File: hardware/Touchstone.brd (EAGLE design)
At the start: 50.8 x 50.8 mm, 69 parts, among them J3 USB-MICROB, U1 NEOPIXEL_NANO_2427, U10 TSL2591, U11 915MHz, U12 MH-Z19, U13 CCS811-I2C, U14 IAQ-CORE-C, U15 VLP-450-F, U16 VLP-450-F, U2 FT231XQ-R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

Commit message: Added pullups on CCS811's signal lines
RESET AND WAKE lines pulled up by default
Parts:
- added R12, R14: 100K, Adafruit Feather 32u4 Bluefruit LE:MICROBUILDER__0402MP
- moved U13 0.25 mm to (40.2, 1.06)
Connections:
- new net N$6: R12.2, U13.2
- net D5: now also R14.2
- net VCC: now also R12.1, R14.1
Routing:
- net VCC: track 199.8 -> 212.9 mm, vias 7 -> 8
- net D5: track 42.6 -> 47.8 mm, vias 2 -> 3
- net N$6: track 0.00 -> 5.14 mm
- net N$13: track 11.6 -> 11.0 mm
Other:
- board text added: "v0.57 | August 2017"
- board text removed: "v0.56b | July 2017"

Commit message: Added SMD pads for T/RH breakout
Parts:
- added U$6: CONN_HDR_1.27MM_SMD_4POS, CONN_HDR_1.27MM_SMD_4POS:CONN_HDR_1.27MM_SMD_4POS
- moved U$3 17.5 mm to (33.5, 47.4)
- moved C16 6.83 mm to (45.7, 38.3)
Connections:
- net GND: now also U$6.P$4
- net SCL: now also U$6.P$2
- net SDA: now also U$6.P$3
- net VCC: now also U$6.P$1
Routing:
- net GND: track 21.3 -> 16.1 mm
- net VCC: track 212.9 -> 217.7 mm
- net SCL: track 165.8 -> 170.2 mm
- net SDA: track 160.1 -> 162.3 mm

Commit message: Version number change; minor adjustments
- Changed version number to 0.5.7 (new versioning format)
- silkscreen adjustments
- some schematic rearrangements
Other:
- board text added: "v0.5.7 | August 2017"
- board text removed: "v0.57 | August 2017"
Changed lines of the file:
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@@
 <text x="4.699" y="19.8628" size="1.016" layer="122" font="vector" ratio="16" rot="MR90" align="center-left">Touchstone</text>
 <text x="30.9372" y="49.5046" size="0.6096" layer="122" font="vector" rot="MR0">Designed by Akram Ali</text>
-<text x="3.0988" y="19.939" size="0.6096" layer="122" font="vector" rot="MR90">v0.57 | August 2017</text>
+<text x="3.0988" y="19.939" size="0.6096" layer="122" font="vector" rot="MR90">v0.5.7 | August 2017</text>
 <text x="2.5654" y="19.939" size="0.8128" layer="122" font="vector" ratio="12" rot="MR270" align="bottom-right">crtlabs.org</text>
 <rectangle x1="1.3462" y1="12.8524" x2="1.7526" y2="12.9032" layer="122" rot="R90"/>
@@
 </element>
 <element name="R14" library="Adafruit Feather 32u4 Bluefruit LE" package="MICROBUILDER__0402MP" value="100K" x="31.6484" y="2.3622" smashed="yes" rot="R180">
-<attribute name="NAME" x="31.75" y="1.8605" size="0.6096" layer="121" font="vector" rot="R180" align="bottom-center"/>
+<attribute name="NAME" x="31.7246" y="3.4607" size="0.6096" layer="121" font="vector" rot="R180" align="bottom-center"/>
 </element>
 <element name="U$6" library="CONN_HDR_1.27MM_SMD_4POS" package="CONN_HDR_1.27MM_SMD_4POS" value="CONN_HDR_1.27MM_SMD_4POS" x="45.2882" y="43.1038"/>

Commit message: Added reset button
- added momentary tactile button for resetting device (reconfiguring,
not power cycle)
- added other circuitry for button
- moved I2C headers to make space for reset button
- several traces redone to accomodate button
- minor silkscreen adjustment
- DRC/ERC checked
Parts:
- added C8: 0.1uF, Adafruit Feather 32u4 Bluefruit LE:MICROBUILDER__0402MP
- added R16, R21: 10K, Adafruit Feather 32u4 Bluefruit LE:MICROBUILDER__0402MP
- added S1: MOMENTARY-SWITCH-SPST-SMD-6.0X3.5MM, SparkFun-Switches:TACTILE_SWITCH_SMD_6.0X3.5MM
- moved J1 15.2 mm to (2.03, 25.4)
- moved U$1 3.07 mm to (5.94, 48.5)
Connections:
- new net N$7: R16.1, R21.2, S1.2
- net A1: now also C8.2, R21.1
- net GND: now also C8.1, S1.1
- net VCC: now also R16.2
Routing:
- net A1: track 0.00 -> 110.5 mm, vias 0 -> 4
- net VCC: track 217.7 -> 241.2 mm, vias 8 -> 10
- net SCL: track 170.2 -> 162.7 mm
- net SDA: track 162.3 -> 155.7 mm, vias 8 -> 6
- net D5: track 47.8 -> 52.7 mm
- net N$7: track 0.00 -> 4.41 mm
- net PWR: track 87.1 -> 87.8 mm, vias 3 -> 4
- net GND: vias 46 -> 47

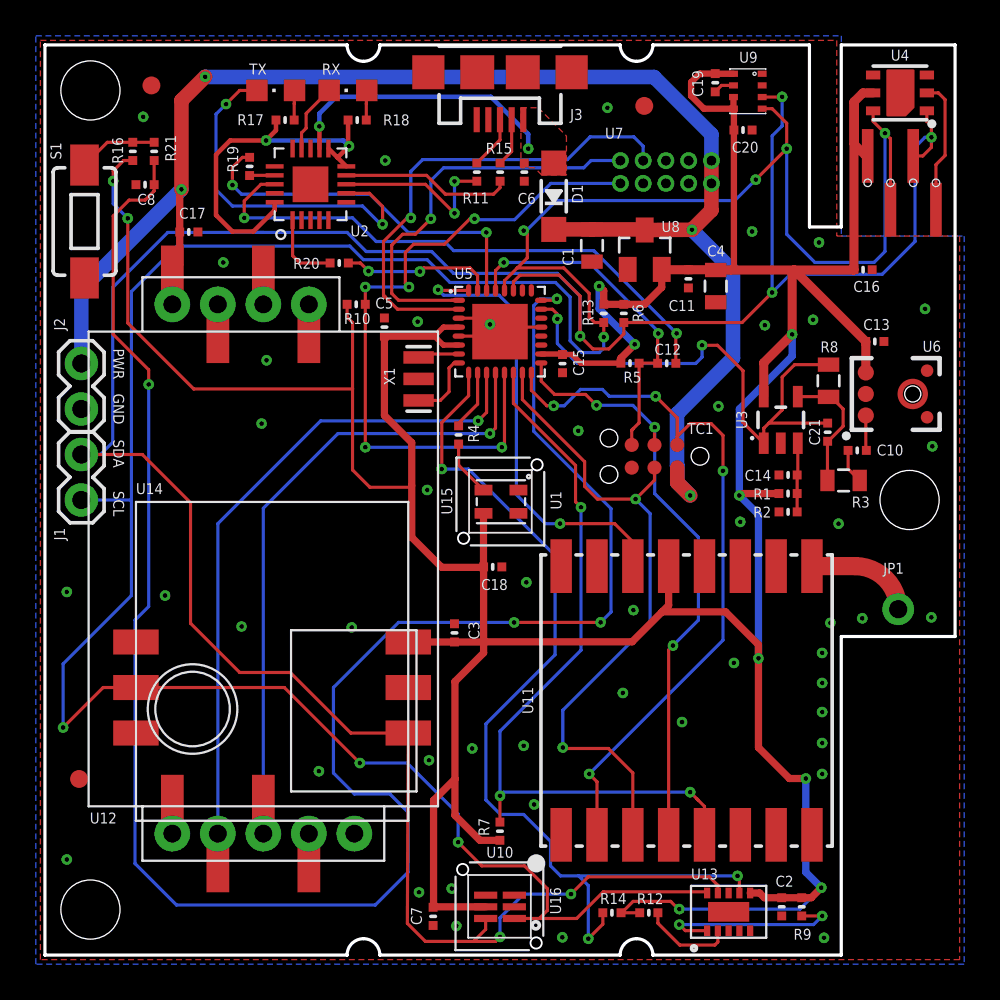
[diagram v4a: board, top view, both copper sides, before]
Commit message: Several routing adjustments
- PMS7003 TX rewired from D3 to A1 (D3 is INT pin)
- Button reqired from A1 to D3 (same reason above)
- adjusted several traces to account for the above rewiring
- Added several GND vias under MCU and FTDI (heatsink - may help a tiny
bit)
- minor silkscreen adjustments to account for above
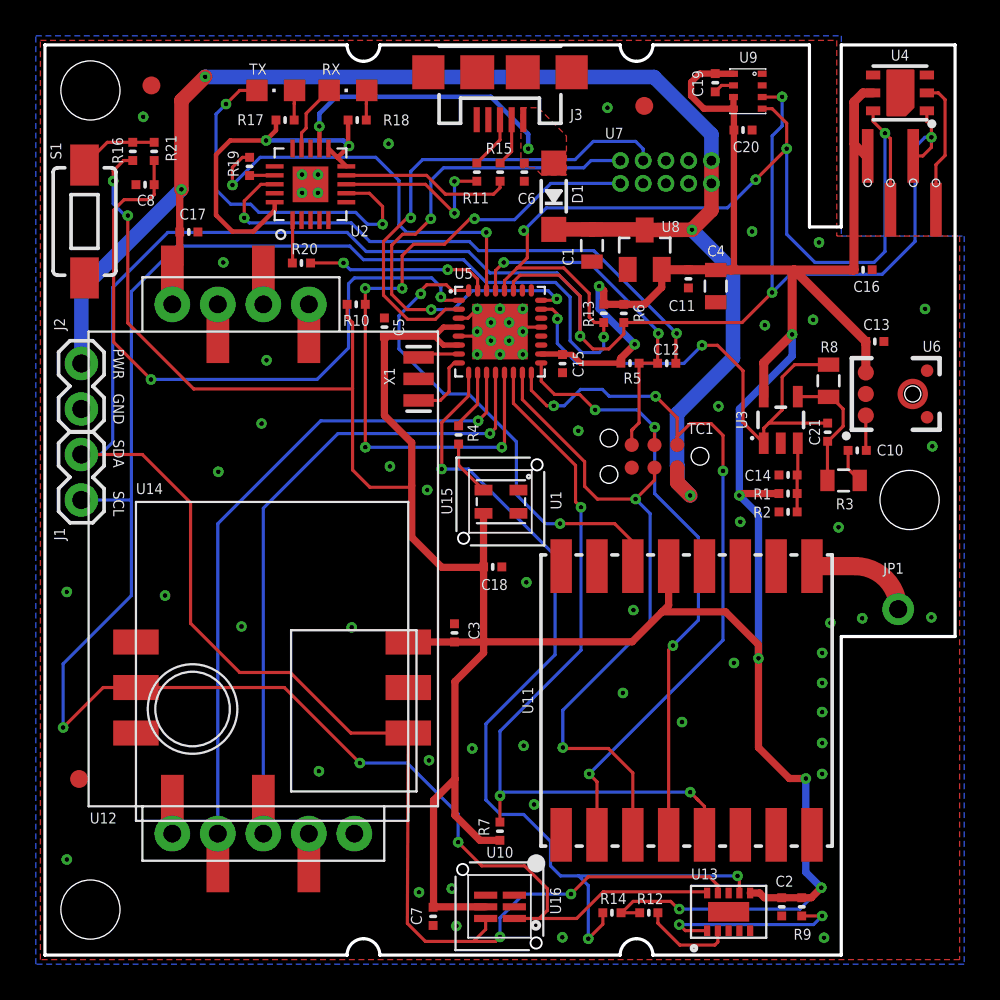
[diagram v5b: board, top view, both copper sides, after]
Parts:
- moved R20 2.11 mm to (14.3, 38.6)
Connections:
- net A1: now also U7.9; no longer C8.2, R21.1
- net D3: now also C8.2, R21.1; no longer U7.9
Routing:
- net A1: track 110.5 -> 29.8 mm, vias 4 -> 3
- net D3: track 23.0 -> 37.3 mm, vias 1 -> 2
- net GND: track 16.1 -> 12.9 mm, vias 47 -> 63
- net RX: track 20.7 -> 23.4 mm
- net N$2: track 4.25 -> 2.40 mm
- net TX: track 8.50 -> 10.3 mm
- net SDA: track 155.7 -> 154.0 mm
- net D2: track 25.8 -> 27.3 mm

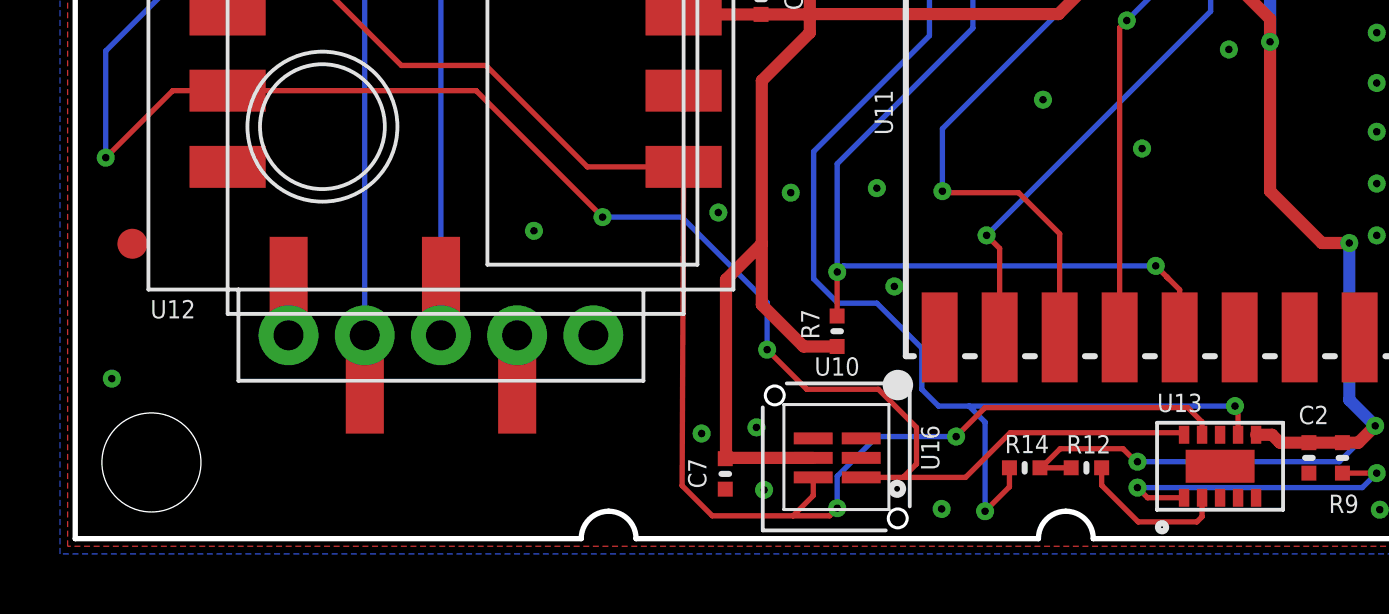
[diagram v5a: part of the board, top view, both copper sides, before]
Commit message: Added another fiducial marker
- rearranged fiducials a bit
- minor schematic update
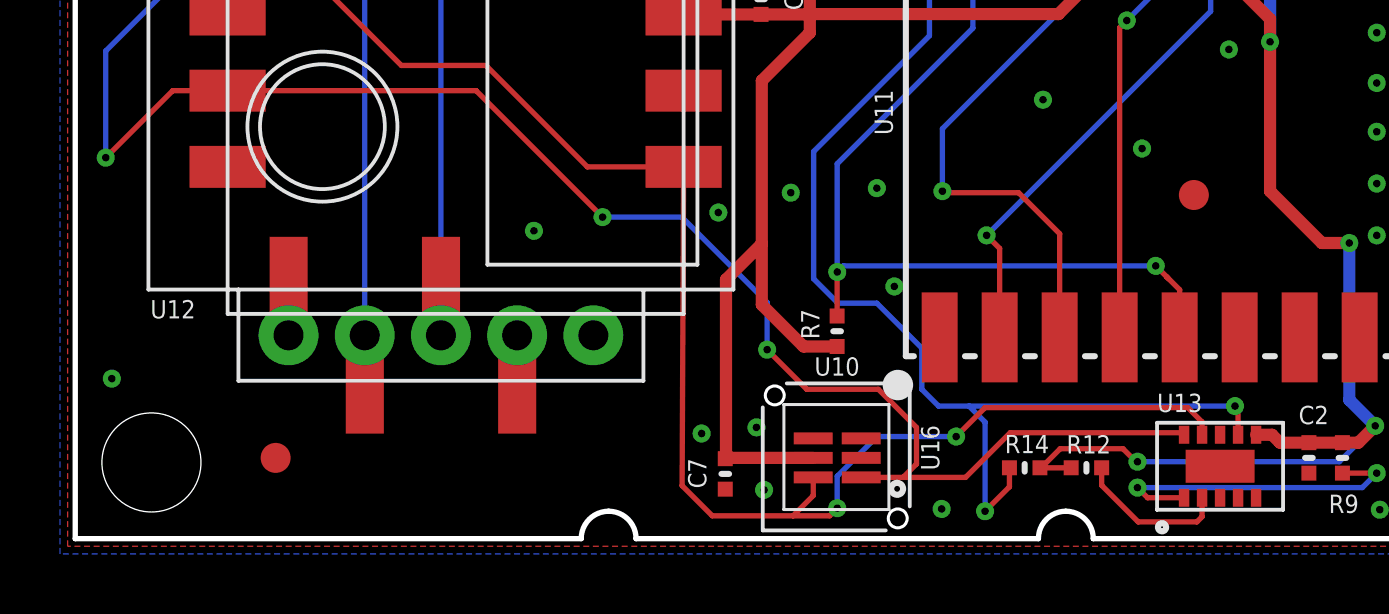
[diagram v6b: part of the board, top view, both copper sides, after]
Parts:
- added U$7: FIDUCIAL, adafruit:FIDUCIAL_1MM
- moved U$2 8.59 mm to (6.68, 2.69)
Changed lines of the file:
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@@
 <element name="H2" library="SparkFun-Electromechanical" package="STAND-OFF" value="STAND-OFF" x="2.54" y="2.54" smashed="yes"/>
 <element name="U$1" library="adafruit" package="FIDUCIAL_1MM" value="FIDUCIAL" x="5.9436" y="48.5394"/>
-<element name="U$2" library="adafruit" package="FIDUCIAL_1MM" value="FIDUCIAL" x="1.905" y="9.8298"/>
+<element name="U$2" library="adafruit" package="FIDUCIAL_1MM" value="FIDUCIAL" x="6.6802" y="2.6924"/>
 <element name="U$3" library="adafruit" package="FIDUCIAL_1MM" value="FIDUCIAL" x="33.4518" y="47.3964"/>
 <element name="U10" library="TSL2591" package="DFN6_TAOS" value="TSL2591" x="25.4" y="2.6924" smashed="yes" rot="R180">
@@
 <attribute name="NAME" x="7.3469" y="45.0342" size="0.6096" layer="121" font="vector" rot="R90" align="bottom-center"/>
 </element>
+<element name="U$7" library="adafruit" package="FIDUCIAL_1MM" value="FIDUCIAL" x="37.2872" y="11.4554"/>
 </elements>
 <signals>
